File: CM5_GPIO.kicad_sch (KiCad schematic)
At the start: 16 parts, among them J14 JST_SHBM04B-SRSS-TB, J2 Conn_02x07_Odd_Even, J3 Conn_01x03, J8 THD-20-R, SW1 Right angle Tact button, U5 74LVC1G07SE-7

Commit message: Removing unwanted sections, such that the carrier board is a blank canvas
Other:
- title: Compute Module 5 IO Board - GPIO - Ethernet -> Compute Module 5 IO Board
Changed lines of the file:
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@@
 	(paper "A4")
 	(title_block
-		(title "Compute Module 5 IO Board - GPIO - Ethernet")
+		(title "Compute Module 5 IO Board")
 		(rev "1")
 		(company "Copyright © 2024 Raspberry Pi Ltd.")

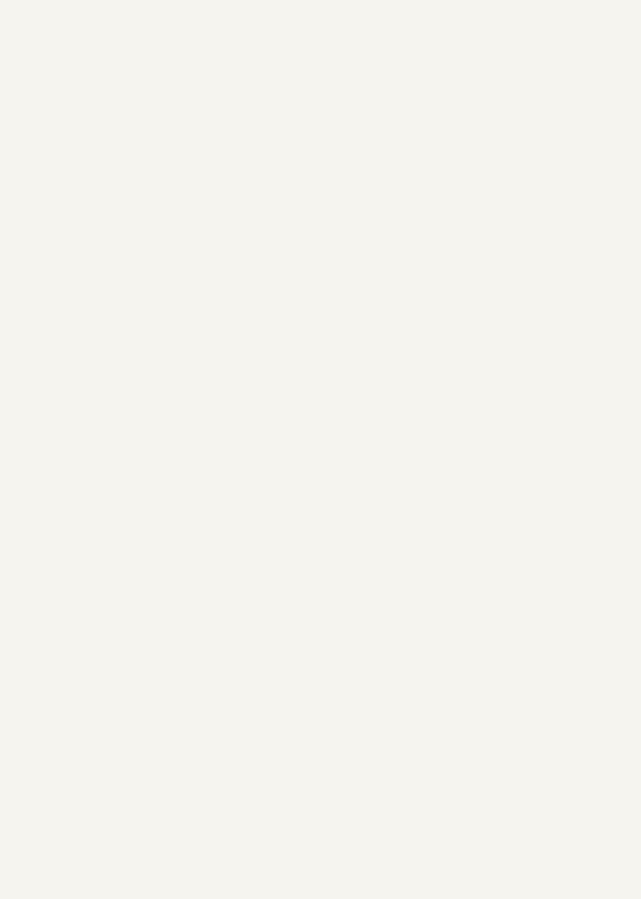
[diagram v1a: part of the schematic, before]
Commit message: Included Cube pilot schematic symbol, pcb footprint and created another sheet.
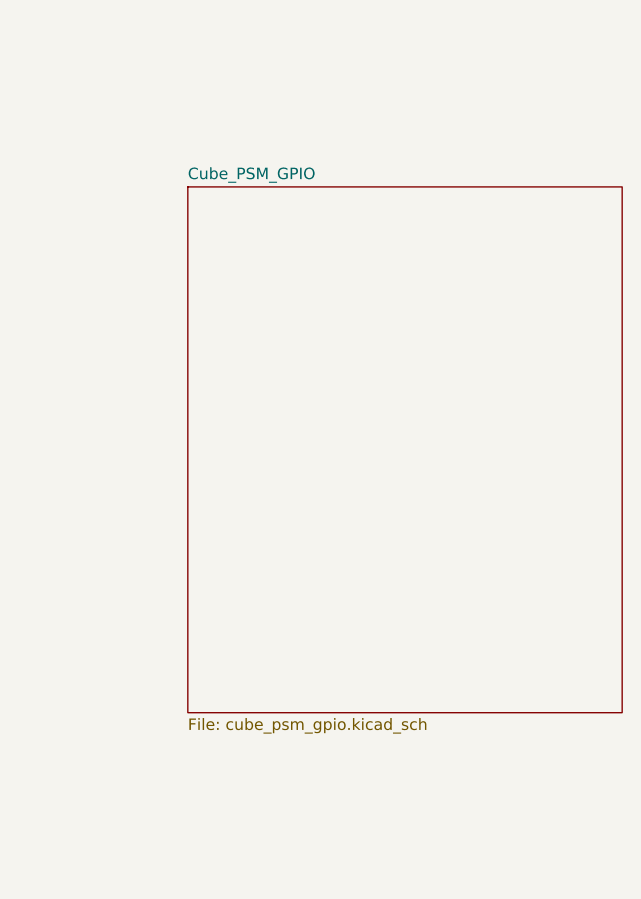
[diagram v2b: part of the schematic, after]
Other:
- added sheet Cube_PSM_GPIO (cube_psm_gpio.kicad_sch)
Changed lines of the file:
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@@
+		)
+	)
+	(sheet
+		(at 214.63 59.69)
+		(size 48.26 58.42)
+		(fields_autoplaced yes)
+		(stroke
+			(width 0.1524)
+			(type solid)
+		)
+		(fill
+			(color 0 0 0 0.0000)
+		)
+		(property "Sheetname" "Cube_PSM_GPIO"
+			(at 214.63 58.9784 0)
+			(effects
+				(font
+					(size 1.27 1.27)
+				)
+				(justify left bottom)
+			)
+		)
+		(property "Sheetfile" "cube_psm_gpio.kicad_sch"
+			(at 214.63 118.6946 0)
+			(effects
+				(font
+					(size 1.27 1.27)
+				)
+				(justify left top)
+			)
+		)
+		(instances
+			(project "CM5IO"
+				(path "/e63e39d7-6ac0-4ffd-8aa3-1841a4541b55/00000000-0000-0000-0000-00005cff706a"
+					(page "5")
+				)
+			)
 		)
 	)
